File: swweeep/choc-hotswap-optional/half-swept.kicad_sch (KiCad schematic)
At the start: 32 parts, among them J1 JST-BATTERY, SW1 SW_Push, SW10 SW_Push, SW11 SW_Push, SW12 SW_Push, SW13 SW_DPDT, SW14 SW_Push, SW15 SW_Push, SW16 SW_Push, SW17 SW_Push, SW18 SW_Push, SW2 SW_Push, SW20 SW_Push, SW21 SW_Push, SW3 SW_Push, SW4 SW_Push, SW5 SW_Push, SW6 SW_Push, SW7 SW_DPDT, SW8 SW_Push, SW9 SW_Push, U1 nice_nano

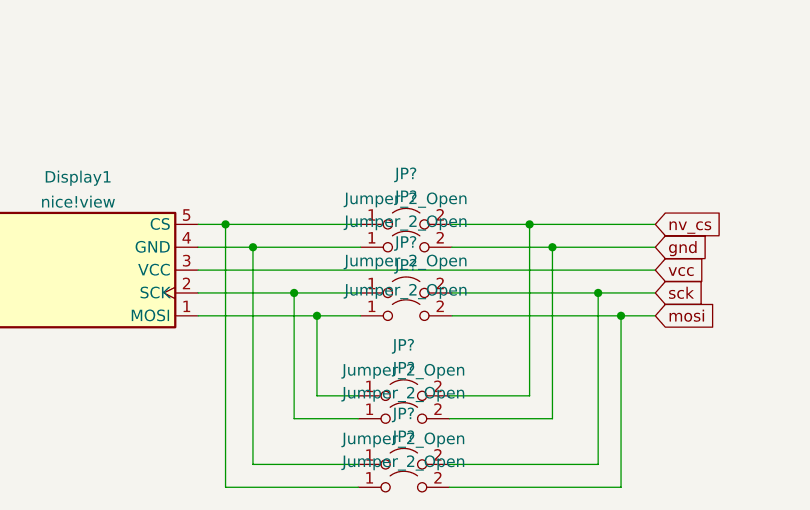
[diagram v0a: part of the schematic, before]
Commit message: updated footprints to have user.drawings for easier svg exports
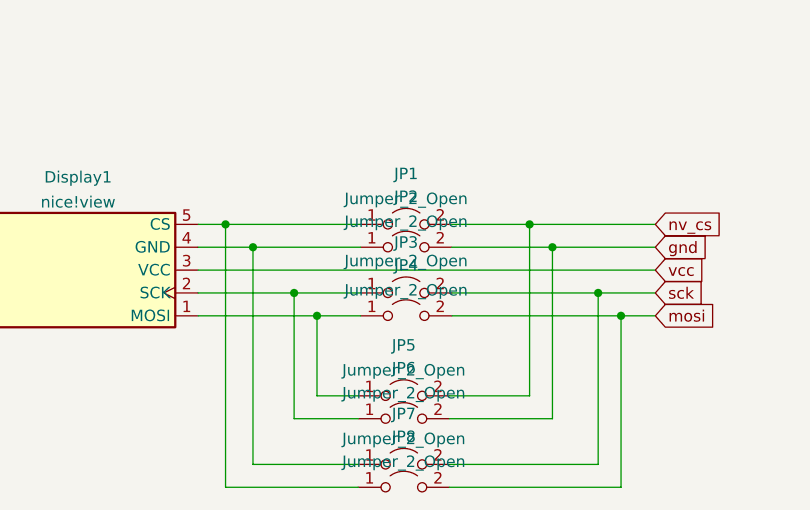
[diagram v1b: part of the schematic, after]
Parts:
- J1: footprint Connector_JST:JST_PH_S3B-PH-K_1x03_P2.00mm_Horizontal -> fingerpunch:JST_PH_S3B-PH-K-keyboard
- gave numbers to parts that had none: 8
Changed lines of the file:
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@@
   (symbol (lib_id "Jumper:Jumper_2_Open") (at 76.2 162.814 0) (unit 1)
     (in_bom yes) (on_board yes) (fields_autoplaced)
-    (property "Reference" "JP?" (id 0) (at 76.2 157.1965 0))
+    (property "Reference" "JP8" (id 0) (at 76.2 157.1965 0))
     (property "Value" "Jumper_2_Open" (id 1) (at 76.2 159.9716 0))
     (property "Footprint" "Jumper:SolderJumper-2_P1.3mm_Open_TrianglePad1.0x1.5mm" (id 2) (at 76.2 162.814 0)
@@
   (symbol (lib_id "Jumper:Jumper_2_Open") (at 76.454 136.144 0) (unit 1)
     (in_bom yes) (on_board yes) (fields_autoplaced)
-    (property "Reference" "JP?" (id 0) (at 76.454 130.5265 0))
+    (property "Reference" "JP2" (id 0) (at 76.454 130.5265 0))
     (property "Value" "Jumper_2_Open" (id 1) (at 76.454 133.3016 0))
     (property "Footprint" "Jumper:SolderJumper-2_P1.3mm_Open_TrianglePad1.0x1.5mm" (id 2) (at 76.454 136.144 0)
@@
   (symbol (lib_id "Jumper:Jumper_2_Open") (at 76.454 133.604 0) (unit 1)
     (in_bom yes) (on_board yes) (fields_autoplaced)
-    (property "Reference" "JP?" (id 0) (at 76.454 127.9865 0))
+    (property "Reference" "JP1" (id 0) (at 76.454 127.9865 0))
     (property "Value" "Jumper_2_Open" (id 1) (at 76.454 130.7616 0))
     (property "Footprint" "Jumper:SolderJumper-2_P1.3mm_Open_TrianglePad1.0x1.5mm" (id 2) (at 76.454 133.604 0)
@@
   (symbol (lib_id "Jumper:Jumper_2_Open") (at 76.2 152.654 0) (unit 1)
     (in_bom yes) (on_board yes) (fields_autoplaced)
-    (property "Reference" "JP?" (id 0) (at 76.2 147.0365 0))
+    (property "Reference" "JP5" (id 0) (at 76.2 147.0365 0))
     (property "Value" "Jumper_2_Open" (id 1) (at 76.2 149.8116 0))
     (property "Footprint" "Jumper:SolderJumper-2_P1.3mm_Open_TrianglePad1.0x1.5mm" (id 2) (at 76.2 152.654 0)
@@
       (effects (font (size 1.27 1.27)) (justify left))
     )
-    (property "Footprint" "Connector_JST:JST_PH_S3B-PH-K_1x03_P2.00mm_Horizontal" (id 2) (at 197.104 121.158 0)
+    (property "Footprint" "fingerpunch:JST_PH_S3B-PH-K-keyboard" (id 2) (at 197.104 121.158 0)
       (effects (font (size 1.27 1.27)) hide)
     )
@@
   (symbol (lib_id "Jumper:Jumper_2_Open") (at 76.454 143.764 0) (unit 1)
     (in_bom yes) (on_board yes) (fields_autoplaced)
-    (property "Reference" "JP?" (id 0) (at 76.454 138.1465 0))
+    (property "Reference" "JP4" (id 0) (at 76.454 138.1465 0))
     (property "Value" "Jumper_2_Open" (id 1) (at 76.454 140.9216 0))
     (property "Footprint" "Jumper:SolderJumper-2_P1.3mm_Open_TrianglePad1.0x1.5mm" (id 2) (at 76.454 143.764 0)
@@
   (symbol (lib_id "Jumper:Jumper_2_Open") (at 76.454 141.224 0) (unit 1)
     (in_bom yes) (on_board yes)
-    (property "Reference" "JP?" (id 0) (at 76.454 135.6065 0))
+    (property "Reference" "JP3" (id 0) (at 76.454 135.6065 0))
     (property "Value" "Jumper_2_Open" (id 1) (at 76.454 137.668 0))
     (property "Footprint" "Jumper:SolderJumper-2_P1.3mm_Open_TrianglePad1.0x1.5mm" (id 2) (at 76.454 141.224 0)
@@
   (symbol (lib_id "Jumper:Jumper_2_Open") (at 76.2 160.274 0) (unit 1)
     (in_bom yes) (on_board yes) (fields_autoplaced)
-    (property "Reference" "JP?" (id 0) (at 76.2 154.6565 0))
+    (property "Reference" "JP7" (id 0) (at 76.2 154.6565 0))
     (property "Value" "Jumper_2_Open" (id 1) (at 76.2 157.4316 0))
     (property "Footprint" "Jumper:SolderJumper-2_P1.3mm_Open_TrianglePad1.0x1.5mm" (id 2) (at 76.2 160.274 0)
@@
   (symbol (lib_id "Jumper:Jumper_2_Open") (at 76.2 155.194 0) (unit 1)
     (in_bom yes) (on_board yes) (fields_autoplaced)
-    (property "Reference" "JP?" (id 0) (at 76.2 149.5765 0))
+    (property "Reference" "JP6" (id 0) (at 76.2 149.5765 0))
     (property "Value" "Jumper_2_Open" (id 1) (at 76.2 152.3516 0))
     (property "Footprint" "Jumper:SolderJumper-2_P1.3mm_Open_TrianglePad1.0x1.5mm" (id 2) (at 76.2 155.194 0)
@@
     )
     (path "/aa53b0fd-9b14-4a92-a45a-1b2e04648b9e"
-      (reference "J1") (unit 1) (value "JST-BATTERY") (footprint "Connector_JST:JST_PH_S3B-PH-K_1x03_P2.00mm_Horizontal")
+      (reference "J1") (unit 1) (value "JST-BATTERY") (footprint "fingerpunch:JST_PH_S3B-PH-K-keyboard")
+    )
+    (path "/9e675945-b3ef-45fc-b0c0-ae7d5196314f"
+      (reference "JP1") (unit 1) (value "Jumper_2_Open") (footprint "Jumper:SolderJumper-2_P1.3mm_Open_TrianglePad1.0x1.5mm")
+    )
+    (path "/467f624c-97ea-450a-8a29-84010edf11b2"
+      (reference "JP2") (unit 1) (value "Jumper_2_Open") (footprint "Jumper:SolderJumper-2_P1.3mm_Open_TrianglePad1.0x1.5mm")
+    )
+    (path "/cf11df2f-d54e-43bb-aae6-bcc998f1ace1"
+      (reference "JP3") (unit 1) (value "Jumper_2_Open") (footprint "Jumper:SolderJumper-2_P1.3mm_Open_TrianglePad1.0x1.5mm")
+    )
+    (path "/c5f462c4-5085-48e6-be04-f1c472750918"
+      (reference "JP4") (unit 1) (value "Jumper_2_Open") (footprint "Jumper:SolderJumper-2_P1.3mm_Open_TrianglePad1.0x1.5mm")
+    )
+    (path "/9f81a0ad-91a9-4222-a816-8428cdcec98c"
+      (reference "JP5") (unit 1) (value "Jumper_2_Open") (footprint "Jumper:SolderJumper-2_P1.3mm_Open_TrianglePad1.0x1.5mm")
+    )
+    (path "/f767c241-0d2a-4a60-af21-e950fbb9f412"
+      (reference "JP6") (unit 1) (value "Jumper_2_Open") (footprint "Jumper:SolderJumper-2_P1.3mm_Open_TrianglePad1.0x1.5mm")
+    )
+    (path "/d1900729-d56b-4976-aa55-9cc260dc60e7"
+      (reference "JP7") (unit 1) (value "Jumper_2_Open") (footprint "Jumper:SolderJumper-2_P1.3mm_Open_TrianglePad1.0x1.5mm")
     )
     (path "/0b93f6f6-8a82-473c-8f29-17cf3f741034"
-      (reference "JP?") (unit 1) (value "Jumper_2_Open") (footprint "Jumper:SolderJumper-2_P1.3mm_Open_TrianglePad1.0x1.5mm")
-    )
-    (path "/467f624c-97ea-450a-8a29-84010edf11b2"
-      (reference "JP?") (unit 1) (value "Jumper_2_Open") (footprint "Jumper:SolderJumper-2_P1.3mm_Open_TrianglePad1.0x1.5mm")
-    )
-    (path "/9e675945-b3ef-45fc-b0c0-ae7d5196314f"
-      (reference "JP?") (unit 1) (value "Jumper_2_Open") (footprint "Jumper:SolderJumper-2_P1.3mm_Open_TrianglePad1.0x1.5mm")
-    )
-    (path "/9f81a0ad-91a9-4222-a816-8428cdcec98c"
-      (reference "JP?") (unit 1) (value "Jumper_2_Open") (footprint "Jumper:SolderJumper-2_P1.3mm_Open_TrianglePad1.0x1.5mm")
-    )
-    (path "/c5f462c4-5085-48e6-be04-f1c472750918"
-      (reference "JP?") (unit 1) (value "Jumper_2_Open") (footprint "Jumper:SolderJumper-2_P1.3mm_Open_TrianglePad1.0x1.5mm")
-    )
-    (path "/cf11df2f-d54e-43bb-aae6-bcc998f1ace1"
-      (reference "JP?") (unit 1) (value "Jumper_2_Open") (footprint "Jumper:SolderJumper-2_P1.3mm_Open_TrianglePad1.0x1.5mm")
-    )
-    (path "/d1900729-d56b-4976-aa55-9cc260dc60e7"
-      (reference "JP?") (unit 1) (value "Jumper_2_Open") (footprint "Jumper:SolderJumper-2_P1.3mm_Open_TrianglePad1.0x1.5mm")
-    )
-    (path "/f767c241-0d2a-4a60-af21-e950fbb9f412"
-      (reference "JP?") (unit 1) (value "Jumper_2_Open") (footprint "Jumper:SolderJumper-2_P1.3mm_Open_TrianglePad1.0x1.5mm")
+      (reference "JP8") (unit 1) (value "Jumper_2_Open") (footprint "Jumper:SolderJumper-2_P1.3mm_Open_TrianglePad1.0x1.5mm")
     )
     (path "/00000000-0000-0000-0000-0000604ea4f3"

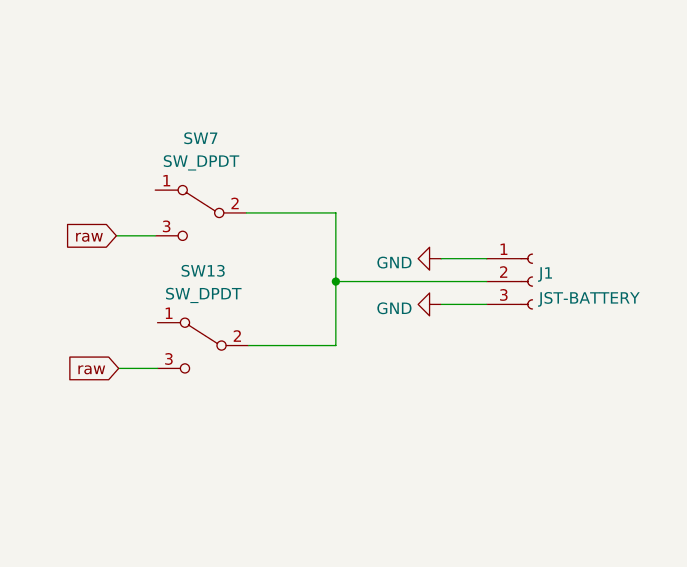
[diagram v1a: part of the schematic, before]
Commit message: fixed unconnected battery ground and updated readme with pics
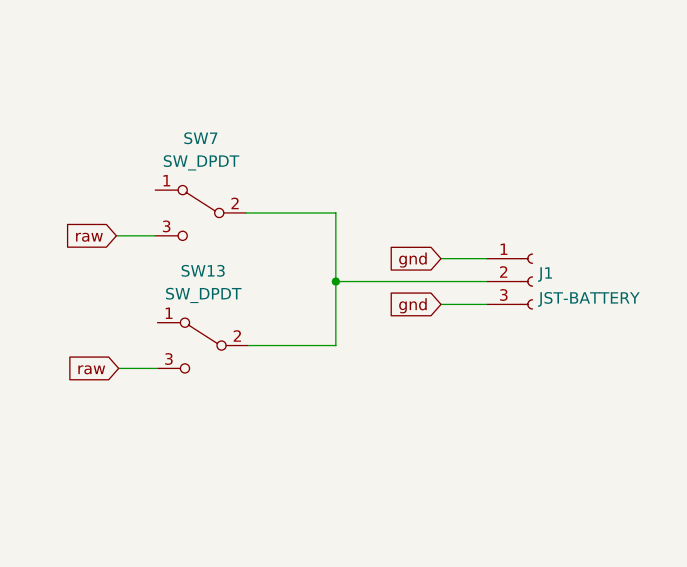
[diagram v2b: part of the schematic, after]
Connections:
- net GND is gone; now on net gnd: J1.1 (Pin_1), J1.3 (Pin_3)
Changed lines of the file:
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@@
+    )
+  )
+  (global_label "gnd" (shape input) (at 186.944 118.618 180) (fields_autoplaced)
+    (effects (font (size 1.27 1.27)) (justify right))
+    (property "Intersheet References" "${INTERSHEET_REFS}" (id 0) (at 181.1727 118.5386 0)
+      (effects (font (size 1.27 1.27)) (justify right) hide)
     )
   )
@@
     (property "Intersheet References" "${INTERSHEET_REFS}" (id 0) (at 0 0 0)
       (effects (font (size 1.27 1.27)) hide)
+    )
+  )
+  (global_label "gnd" (shape input) (at 186.944 123.698 180) (fields_autoplaced)
+    (effects (font (size 1.27 1.27)) (justify right))
+    (property "Intersheet References" "${INTERSHEET_REFS}" (id 0) (at 181.1727 123.6186 0)
+      (effects (font (size 1.27 1.27)) (justify right) hide)
     )
   )
@@
     (pin "2")
   )
-  (symbol (lib_id "power:GND") (at 186.944 123.698 270) (unit 1)
-    (in_bom yes) (on_board yes) (fields_autoplaced)
-    (property "Reference" "#PWR0102" (id 0) (at 180.594 123.698 0)
-      (effects (font (size 1.27 1.27)) hide)
-    )
-    (property "Value" "GND" (id 1) (at 183.7691 124.177 90)
-      (effects (font (size 1.27 1.27)) (justify right))
-    )
-    (property "Footprint" "" (id 2) (at 186.944 123.698 0)
-      (effects (font (size 1.27 1.27)) hide)
-    )
-    (property "Datasheet" "" (id 3) (at 186.944 123.698 0)
-      (effects (font (size 1.27 1.27)) hide)
-    )
-    (pin "1")
-  )
   (symbol (lib_id "jiran-ble:SW_DPDT") (at 159.004 113.538 0) (mirror y) (unit 1)
     (in_bom yes) (on_board yes)
@@
     (pin "2")
   )
-  (symbol (lib_id "power:GND") (at 186.944 118.618 270) (unit 1)
-    (in_bom yes) (on_board yes) (fields_autoplaced)
-    (property "Reference" "#PWR0101" (id 0) (at 180.594 118.618 0)
-      (effects (font (size 1.27 1.27)) hide)
-    )
-    (property "Value" "GND" (id 1) (at 183.7691 119.097 90)
-      (effects (font (size 1.27 1.27)) (justify right))
-    )
-    (property "Footprint" "" (id 2) (at 186.944 118.618 0)
-      (effects (font (size 1.27 1.27)) hide)
-    )
-    (property "Datasheet" "" (id 3) (at 186.944 118.618 0)
-      (effects (font (size 1.27 1.27)) hide)
-    )
-    (pin "1")
-  )
   (symbol (lib_id "Jumper:Jumper_2_Open") (at 76.2 155.194 0) (unit 1)
     (in_bom yes) (on_board yes) (fields_autoplaced)
@@
   )
   (symbol_instances
-    (path "/f642ee47-88ea-4601-9420-1516c4b63a85"
-      (reference "#PWR0101") (unit 1) (value "GND") (footprint "")
-    )
-    (path "/5929a13c-96f9-4241-b1f6-89da37f6921a"
-      (reference "#PWR0102") (unit 1) (value "GND") (footprint "")
-    )
     (path "/89cfd60b-fa56-404e-a3a3-e989c1746e33"
       (reference "Display1") (unit 1) (value "nice!view") (footprint "fingerpunch:nice_view")

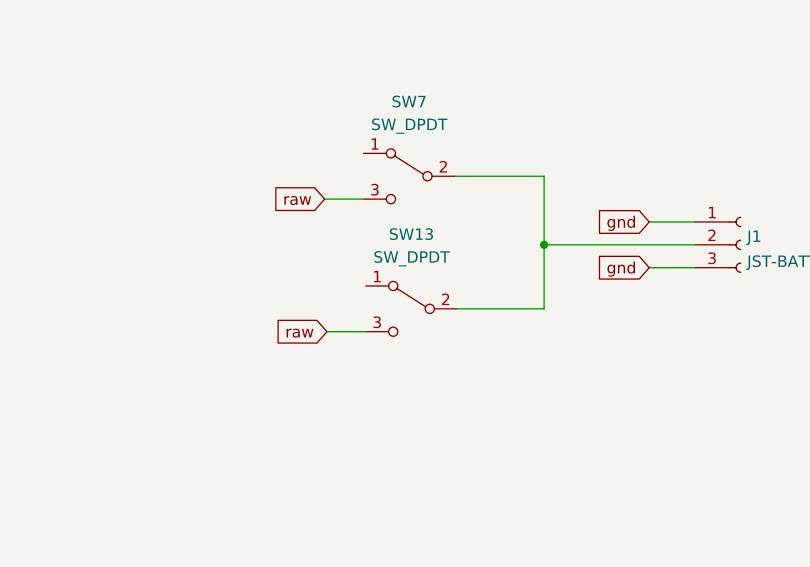
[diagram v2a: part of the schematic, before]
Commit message: replaced on off switch, from MSK12C02 to OS102011MA1QN1
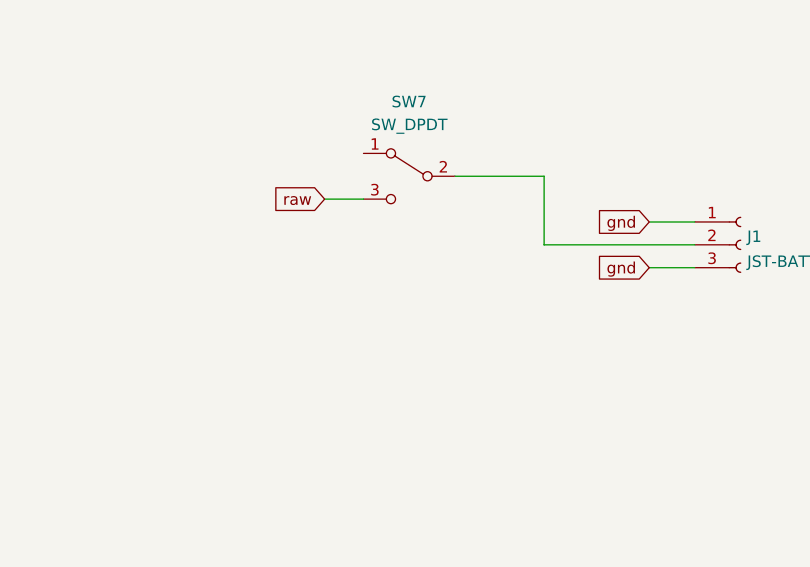
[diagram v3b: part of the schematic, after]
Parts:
- removed SW13: SW_DPDT, fingerpunch:MSK-12C02, symbol jiran-ble:SW_DPDT
- SW7: footprint fingerpunch:MSK-12C02 -> fingerpunch:SW_CuK_OS102011MA1QN1_SPDT_Angled
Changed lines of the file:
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@@
   (junction (at 66.548 143.764) (diameter 0) (color 0 0 0 0)
   )
-  (junction (at 175.26 121.158) (diameter 0) (color 0 0 0 0)
-  )
   (junction (at 100.33 143.764) (diameter 0) (color 0 0 0 0)
   )
@@
   (junction (at 90.17 133.604) (diameter 0) (color 0 0 0 0)
   )
-  (wire (pts (xy 151.13 130.81) (xy 155.448 130.81))
-    (stroke (width 0) (type default) (color 0 0 0 0))
-  )
   (wire (pts (xy 100.33 143.764) (xy 100.33 162.814))
     (stroke (width 0) (type default) (color 0 0 0 0))
@@
     (stroke (width 0) (type default) (color 0 0 0 0))
   )
-  (wire (pts (xy 175.26 121.158) (xy 175.26 128.27))
-    (stroke (width 0) (type default) (color 0 0 0 0))
-  )
   (wire (pts (xy 81.534 141.224) (xy 97.79 141.224))
     (stroke (width 0) (type default) (color 0 0 0 0))
@@
   )
   (wire (pts (xy 53.34 136.144) (xy 59.436 136.144))
-    (stroke (width 0) (type default) (color 0 0 0 0))
-  )
-  (wire (pts (xy 175.26 128.27) (xy 165.608 128.27))
     (stroke (width 0) (type default) (color 0 0 0 0))
   )
@@
     (effects (font (size 1.27 1.27)) (justify right))
     (property "Intersheet References" "${INTERSHEET_REFS}" (id 0) (at 0 0 0)
-      (effects (font (size 1.27 1.27)) hide)
-    )
-  )
-  (global_label "raw" (shape input) (at 151.13 130.81 180) (fields_autoplaced)
-    (effects (font (size 1.27 1.27)) (justify right))
-    (property "Intersheet References" "${INTERSHEET_REFS}" (id 0) (at 345.44 166.37 0)
       (effects (font (size 1.27 1.27)) hide)
     )
@@
     (property "Reference" "SW7" (id 0) (at 160.274 105.283 0))
     (property "Value" "SW_DPDT" (id 1) (at 160.274 107.823 0))
-    (property "Footprint" "fingerpunch:MSK-12C02" (id 2) (at 158.369 105.918 0)
+    (property "Footprint" "fingerpunch:SW_CuK_OS102011MA1QN1_SPDT_Angled" (id 2) (at 158.369 105.918 0)
       (effects (font (size 1.27 1.27)) hide)
     )
@@
     )
     (property "LCSC" "C431540" (id 4) (at 159.004 113.538 0)
-      (effects (font (size 1.27 1.27)) hide)
-    )
-    (pin "1")
-    (pin "2")
-    (pin "3")
-  )
-  (symbol (lib_id "jiran-ble:SW_DPDT") (at 159.258 128.27 0) (mirror y) (unit 1)
-    (in_bom yes) (on_board yes)
-    (property "Reference" "SW13" (id 0) (at 160.528 120.015 0))
-    (property "Value" "SW_DPDT" (id 1) (at 160.528 122.555 0))
-    (property "Footprint" "fingerpunch:MSK-12C02" (id 2) (at 158.623 120.65 0)
-      (effects (font (size 1.27 1.27)) hide)
-    )
-    (property "Datasheet" "" (id 3) (at 158.623 120.65 0)
-      (effects (font (size 1.27 1.27)) hide)
-    )
-    (property "LCSC" "C431540" (id 4) (at 159.258 128.27 0)
       (effects (font (size 1.27 1.27)) hide)
     )
@@
     )
     (path "/764570c2-a63f-40d9-bd89-9de3cab3ff49"
-      (reference "SW7") (unit 1) (value "SW_DPDT") (footprint "fingerpunch:MSK-12C02")
+      (reference "SW7") (unit 1) (value "SW_DPDT") (footprint "fingerpunch:SW_CuK_OS102011MA1QN1_SPDT_Angled")
     )
     (path "/00000000-0000-0000-0000-0000604a6c6c"
@@
       (reference "SW12") (unit 1) (value "SW_Push") (footprint "fingerpunch:Kailh_socket_PG1350_optional_reversible_millmax")
     )
-    (path "/86051a60-18a2-4d3f-bde8-435d97aaaf3f"
-      (reference "SW13") (unit 1) (value "SW_DPDT") (footprint "fingerpunch:MSK-12C02")
-    )
     (path "/00000000-0000-0000-0000-0000604bad64"
